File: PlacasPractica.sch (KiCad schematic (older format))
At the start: 66 parts, among them J1 USB_OTG, J2 Conn_01x10, J3 Conn_01x10, J4 CONN_02X05, SW1 SW_Push, U1 SAMD20J18A-AU, U2 XBEE, U3 MB85RC64VPNF-G-JNERE1, U4 XC6220B331MR-G, U5 XC6220B331MR-G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

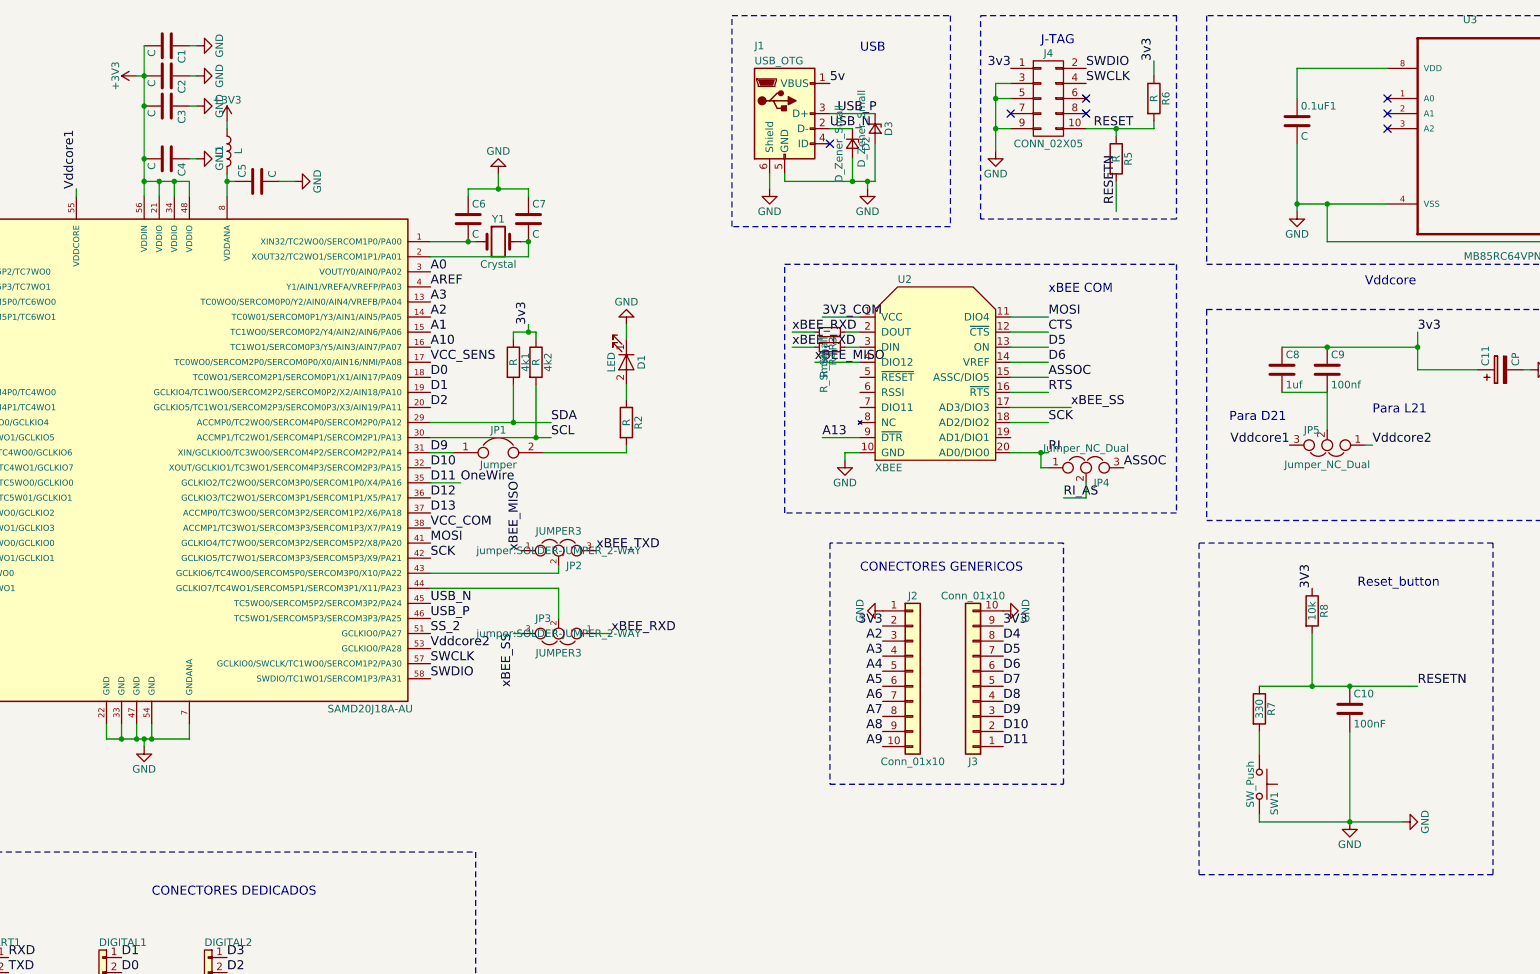
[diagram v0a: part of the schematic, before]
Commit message: Inicio diseño PCB
Se ha iniciado con el diseño de la PCB
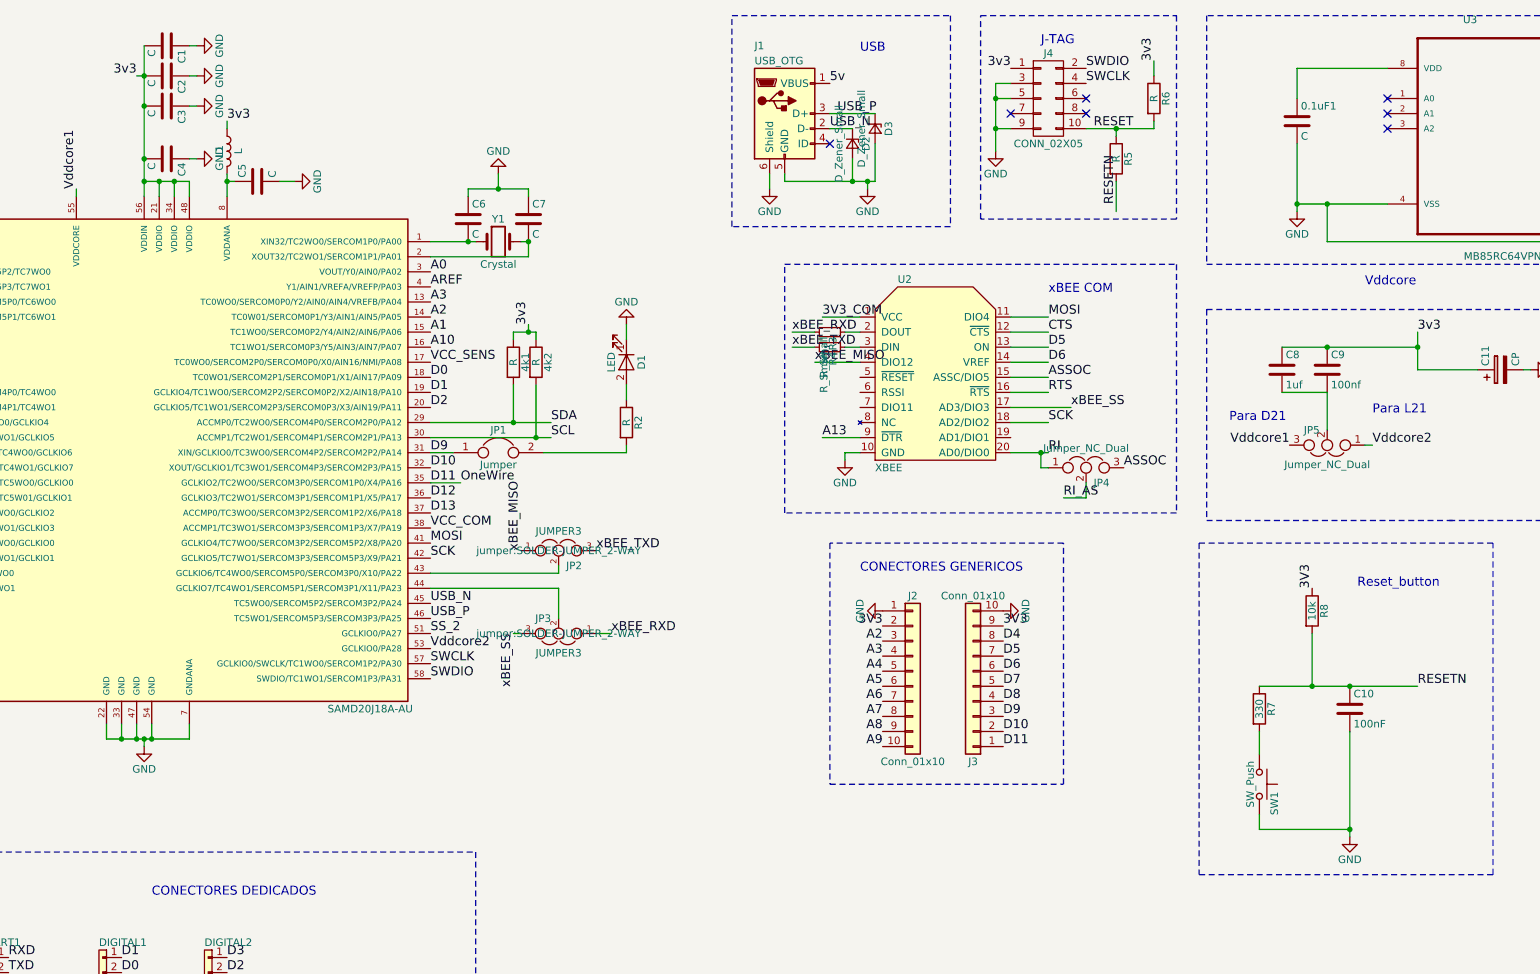
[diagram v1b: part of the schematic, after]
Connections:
- net +3V3 is gone; now on net 3v3: C1.2, C2.2, C3.2, C4.2, L1.1, U1.21 (VDDIO), U1.34 (VDDIO), U1.48 (VDDIO), U1.56 (VDDIN)
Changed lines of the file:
@@
 LIBS:valves
 LIBS:switches
-LIBS:ICs
 LIBS:PlacasPractica-cache
 EELAYER 25 0
@@
 	1    3500 1700
 	0    -1   -1   0
-$EndComp
-$Comp
-L +3V3 #PWR010
-U 1 1 59060D57
-P 2450 1000
-F 0 "#PWR010" H 2450 850 50  0001 C CNN
-F 1 "+3V3" H 2450 1140 50  0000 C CNN
-F 2 "" H 2450 1000 50  0001 C CNN
-F 3 "" H 2450 1000 50  0001 C CNN
-	1    2450 1000
-	0    -1   -1   0
-$EndComp
-$Comp
-L +3V3 #PWR011
-U 1 1 59060D58
-P 3050 1300
-F 0 "#PWR011" H 3050 1150 50  0001 C CNN
-F 1 "+3V3" H 3050 1440 50  0000 C CNN
-F 2 "" H 3050 1300 50  0001 C CNN
-F 3 "" H 3050 1300 50  0001 C CNN
-	1    3050 1300
-	1    0    0    -1
 $EndComp
 Text Label 4400 2300 0    60   ~ 0
@@
 J-TAG
 $Comp
-L GND #PWR012
+L GND #PWR011
 U 1 1 59060D6D
 P 7300 1750
-F 0 "#PWR012" H 7300 1500 50  0001 C CNN
+F 0 "#PWR011" H 7300 1500 50  0001 C CNN
 F 1 "GND" H 7300 1600 50  0000 C CNN
 F 2 "" H 7300 1750 50  0001 C CNN
@@
 USB
 $Comp
-L GND #PWR013
+L GND #PWR012
 U 1 1 59060D71
 P 6650 1750
-F 0 "#PWR013" H 6650 1500 50  0001 C CNN
+F 0 "#PWR012" H 6650 1500 50  0001 C CNN
 F 1 "GND" H 6650 1600 50  0000 C CNN
 F 2 "" H 6650 1750 50  0001 C CNN
@@
 xBEE_MISO
 $Comp
-L GND #PWR014
+L GND #PWR013
 U 1 1 59060D75
 P 7150 3550
-F 0 "#PWR014" H 7150 3300 50  0001 C CNN
+F 0 "#PWR013" H 7150 3300 50  0001 C CNN
 F 1 "GND" H 7150 3400 50  0000 C CNN
 F 2 "" H 7150 3550 50  0001 C CNN
@@
 3V3_SENS
 $Comp
-L GND #PWR015
+L GND #PWR014
 U 1 1 59060D81
 P 1600 7150
-F 0 "#PWR015" H 1600 6900 50  0001 C CNN
+F 0 "#PWR014" H 1600 6900 50  0001 C CNN
 F 1 "GND" H 1600 7000 50  0000 C CNN
 F 2 "" H 1600 7150 50  0001 C CNN
@@
 $EndComp
 $Comp
-L GND #PWR016
+L GND #PWR015
 U 1 1 59060D82
 P 1600 7950
-F 0 "#PWR016" H 1600 7700 50  0001 C CNN
+F 0 "#PWR015" H 1600 7700 50  0001 C CNN
 F 1 "GND" H 1600 7800 50  0000 C CNN
 F 2 "" H 1600 7950 50  0001 C CNN
@@
 	9200 1000 9200 900
 $Comp
-L GND #PWR017
+L GND #PWR016
 U 1 1 59094656
 P 8150 1500
-F 0 "#PWR017" H 8150 1250 50  0001 C CNN
+F 0 "#PWR016" H 8150 1250 50  0001 C CNN
 F 1 "GND" H 8150 1350 50  0000 C CNN
 F 2 "" H 8150 1500 50  0000 C CNN
@@
 $EndComp
 $Comp
-L GND #PWR018
+L GND #PWR017
 U 1 1 5AB3C19A
 P 10150 1900
-F 0 "#PWR018" H 10150 1650 50  0001 C CNN
+F 0 "#PWR017" H 10150 1650 50  0001 C CNN
 F 1 "GND" H 10150 1750 50  0000 C CNN
 F 2 "" H 10150 1900 50  0001 C CNN
@@
 $EndComp
 $Comp
-L GND #PWR019
+L GND #PWR018
 U 1 1 5AB3DAE7
 P 13650 3200
-F 0 "#PWR019" H 13650 2950 50  0001 C CNN
+F 0 "#PWR018" H 13650 2950 50  0001 C CNN
 F 1 "GND" H 13650 3050 50  0000 C CNN
 F 2 "" H 13650 3200 50  0001 C CNN
@@
 VCC_SENS
 $Comp
-L GND #PWR020
+L GND #PWR019
 U 1 1 5AB3DAEE
 P 14200 3200
-F 0 "#PWR020" H 14200 2950 50  0001 C CNN
+F 0 "#PWR019" H 14200 2950 50  0001 C CNN
 F 1 "GND" H 14200 3050 50  0000 C CNN
 F 2 "" H 14200 3200 50  0001 C CNN
@@
 $EndComp
 $Comp
-L GND #PWR021
+L GND #PWR020
 U 1 1 5AB3DAF4
 P 15800 3000
-F 0 "#PWR021" H 15800 2750 50  0001 C CNN
+F 0 "#PWR020" H 15800 2750 50  0001 C CNN
 F 1 "GND" H 15800 2850 50  0000 C CNN
 F 2 "" H 15800 3000 50  0001 C CNN
@@
 Connection ~ 15800 2600
 $Comp
-L +5V #PWR022
+L +5V #PWR021
 U 1 1 5AB3DADB
 P 12900 2500
-F 0 "#PWR022" H 12900 2350 50  0001 C CNN
+F 0 "#PWR021" H 12900 2350 50  0001 C CNN
 F 1 "+5V" H 12900 2640 50  0000 C CNN
 F 2 "" H 12900 2500 50  0001 C CNN
@@
 $EndComp
 $Comp
-L GND #PWR023
+L GND #PWR022
 U 1 1 5AB3F521
 P 14000 1700
-F 0 "#PWR023" H 14000 1450 50  0001 C CNN
+F 0 "#PWR022" H 14000 1450 50  0001 C CNN
 F 1 "GND" H 14000 1550 50  0000 C CNN
 F 2 "" H 14000 1700 50  0001 C CNN
@@
 $EndComp
 $Comp
-L GND #PWR024
+L GND #PWR023
 U 1 1 5AB3F527
 P 15800 1500
-F 0 "#PWR024" H 15800 1250 50  0001 C CNN
+F 0 "#PWR023" H 15800 1250 50  0001 C CNN
 F 1 "GND" H 15800 1350 50  0000 C CNN
 F 2 "" H 15800 1500 50  0001 C CNN
@@
 Connection ~ 15800 1100
 $Comp
-L +5V #PWR025
+L +5V #PWR024
 U 1 1 5AB3F545
 P 12950 850
-F 0 "#PWR025" H 12950 700 50  0001 C CNN
+F 0 "#PWR024" H 12950 700 50  0001 C CNN
 F 1 "+5V" H 12950 990 50  0000 C CNN
 F 2 "" H 12950 850 50  0001 C CNN
@@
 $EndComp
 $Comp
-L GND #PWR026
+L GND #PWR025
 U 1 1 5AB4419D
 P 13650 4700
-F 0 "#PWR026" H 13650 4450 50  0001 C CNN
+F 0 "#PWR025" H 13650 4450 50  0001 C CNN
 F 1 "GND" H 13650 4550 50  0000 C CNN
 F 2 "" H 13650 4700 50  0001 C CNN
@@
 VCC_COM
 $Comp
-L GND #PWR027
+L GND #PWR026
 U 1 1 5AB441A4
 P 14200 4700
-F 0 "#PWR027" H 14200 4450 50  0001 C CNN
+F 0 "#PWR026" H 14200 4450 50  0001 C CNN
 F 1 "GND" H 14200 4550 50  0000 C CNN
 F 2 "" H 14200 4700 50  0001 C CNN
@@
 $EndComp
 $Comp
-L GND #PWR028
+L GND #PWR027
 U 1 1 5AB441AA
 P 15800 4500
-F 0 "#PWR028" H 15800 4250 50  0001 C CNN
+F 0 "#PWR027" H 15800 4250 50  0001 C CNN
 F 1 "GND" H 15800 4350 50  0000 C CNN
 F 2 "" H 15800 4500 50  0001 C CNN
@@
 Connection ~ 15800 4100
 $Comp
-L +5V #PWR029
+L +5V #PWR028
 U 1 1 5AB441C8
 P 12900 4000
-F 0 "#PWR029" H 12900 3850 50  0001 C CNN
+F 0 "#PWR028" H 12900 3850 50  0001 C CNN
 F 1 "+5V" H 12900 4140 50  0000 C CNN
 F 2 "" H 12900 4000 50  0001 C CNN
@@
 $EndComp
 $Comp
-L GND #PWR030
+L GND #PWR029
 U 1 1 5AB48687
 P 3750 7950
-F 0 "#PWR030" H 3750 7700 50  0001 C CNN
+F 0 "#PWR029" H 3750 7700 50  0001 C CNN
 F 1 "GND" H 3750 7800 50  0000 C CNN
 F 2 "" H 3750 7950 50  0001 C CNN
@@
 $EndComp
 $Comp
-L GND #PWR031
+L GND #PWR030
 U 1 1 5AB4B4A0
 P 2350 7950
-F 0 "#PWR031" H 2350 7700 50  0001 C CNN
+F 0 "#PWR030" H 2350 7700 50  0001 C CNN
 F 1 "GND" H 2350 7800 50  0000 C CNN
 F 2 "" H 2350 7950 50  0001 C CNN
@@
 $EndComp
 $Comp
-L GND #PWR032
+L GND #PWR031
 U 1 1 5AB4BF34
 P 3050 7950
-F 0 "#PWR032" H 3050 7700 50  0001 C CNN
+F 0 "#PWR031" H 3050 7700 50  0001 C CNN
 F 1 "GND" H 3050 7800 50  0000 C CNN
 F 2 "" H 3050 7950 50  0001 C CNN
@@
 $EndComp
 $Comp
-L GND #PWR033
+L GND #PWR032
 U 1 1 5AB4C1E2
 P 2350 7150
-F 0 "#PWR033" H 2350 6900 50  0001 C CNN
+F 0 "#PWR032" H 2350 6900 50  0001 C CNN
 F 1 "GND" H 2350 7000 50  0000 C CNN
 F 2 "" H 2350 7150 50  0001 C CNN
@@
 $EndComp
 $Comp
-L GND #PWR034
+L GND #PWR033
 U 1 1 5AB4CC9B
 P 3050 7150
-F 0 "#PWR034" H 3050 6900 50  0001 C CNN
+F 0 "#PWR033" H 3050 6900 50  0001 C CNN
 F 1 "GND" H 3050 7000 50  0000 C CNN
 F 2 "" H 3050 7150 50  0001 C CNN
@@
 	1    0    0    -1
 $EndComp
-$Comp
-L GND #PWR035
-U 1 1 5AB40006
-P 10500 5950
-F 0 "#PWR035" H 10500 5700 50  0001 C CNN
-F 1 "GND" H 10500 5800 50  0000 C CNN
-F 2 "" H 10500 5950 50  0001 C CNN
-F 3 "" H 10500 5950 50  0001 C CNN
-	1    10500 5950
-	1    0    0    -1
-$EndComp
-$Comp
-L GND #PWR036
-U 1 1 5AB40094
-P 10850 5950
-F 0 "#PWR036" H 10850 5700 50  0001 C CNN
-F 1 "GND" H 10850 5800 50  0000 C CNN
-F 2 "" H 10850 5950 50  0001 C CNN
-F 3 "" H 10850 5950 50  0001 C CNN
-	1    10850 5950
-	0    -1   -1   0
-$EndComp
 Wire Wire Line
 	10250 4700 10250 5050
@@
 	9900 5350 9900 5500
 Wire Wire Line
-	9900 5900 9900 5950
-Wire Wire Line
-	9900 5950 10850 5950
-Connection ~ 10500 5950
-Wire Wire Line
-	10500 5350 10500 5950
+	9900 5900 9900 6000
+Wire Wire Line
+	10500 5350 10500 6050
 Text Label 10250 4400 1    60   ~ 0
 3V3
@@
 $EndComp
 $Comp
-L GND #PWR037
+L GND #PWR036
 U 1 1 5AB46D5A
 P 8200 4550
-F 0 "#PWR037" H 8200 4300 50  0001 C CNN
+F 0 "#PWR036" H 8200 4300 50  0001 C CNN
 F 1 "GND" H 8200 4400 50  0000 C CNN
 F 2 "" H 8200 4550 50  0001 C CNN
@@
 $EndComp
 $Comp
-L GND #PWR038
+L GND #PWR037
 U 1 1 5AB470E5
 P 7400 4550
-F 0 "#PWR038" H 7400 4300 50  0001 C CNN
+F 0 "#PWR037" H 7400 4300 50  0001 C CNN
 F 1 "GND" H 7400 4400 50  0000 C CNN
 F 2 "" H 7400 4550 50  0001 C CNN
@@
 Wire Notes Line
 	11900 3950 11150 3950
+Text Label 2450 1000 2    60   ~ 0
+3v3
+Text Label 3050 1300 0    60   ~ 0
+3v3
+$Comp
+L GND #PWR034
+U 1 1 5AB40006
+P 10500 6050
+F 0 "#PWR034" H 10500 5800 50  0001 C CNN
+F 1 "GND" H 10500 5900 50  0000 C CNN
+F 2 "" H 10500 6050 50  0001 C CNN
+F 3 "" H 10500 6050 50  0001 C CNN
+	1    10500 6050
+	1    0    0    -1
+$EndComp
+Wire Wire Line
+	10500 6000 9900 6000
+Connection ~ 10500 6000
 $EndSCHEMATC

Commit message: Diseño pcb, punto intermedio.
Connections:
- net 5v is gone; now on net +5V: J1.1 (VBUS)
- net 3V3: now also 0.1uF1.1, U3.8 (VDD)
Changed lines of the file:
@@
 LIBS:valves
 LIBS:switches
+LIBS:ICs
 LIBS:PlacasPractica-cache
 EELAYER 25 0
@@
 J-TAG
 $Comp
-L GND #PWR011
+L GND #PWR010
 U 1 1 59060D6D
 P 7300 1750
-F 0 "#PWR011" H 7300 1500 50  0001 C CNN
+F 0 "#PWR010" H 7300 1500 50  0001 C CNN
 F 1 "GND" H 7300 1600 50  0000 C CNN
 F 2 "" H 7300 1750 50  0001 C CNN
@@
 USB_N
 NoConn ~ 7050 1450
-Text Label 7050 1050 0    60   ~ 0
-5v
 Text Notes 7250 850  0    60   ~ 0
 USB
 $Comp
-L GND #PWR012
+L GND #PWR011
 U 1 1 59060D71
 P 6650 1750
-F 0 "#PWR012" H 6650 1500 50  0001 C CNN
+F 0 "#PWR011" H 6650 1500 50  0001 C CNN
 F 1 "GND" H 6650 1600 50  0000 C CNN
 F 2 "" H 6650 1750 50  0001 C CNN
@@
 xBEE_MISO
 $Comp
-L GND #PWR013
+L GND #PWR012
 U 1 1 59060D75
 P 7150 3550
-F 0 "#PWR013" H 7150 3300 50  0001 C CNN
+F 0 "#PWR012" H 7150 3300 50  0001 C CNN
 F 1 "GND" H 7150 3400 50  0000 C CNN
 F 2 "" H 7150 3550 50  0001 C CNN
@@
 3V3_SENS
 $Comp
-L GND #PWR014
+L GND #PWR013
 U 1 1 59060D81
 P 1600 7150
-F 0 "#PWR014" H 1600 6900 50  0001 C CNN
+F 0 "#PWR013" H 1600 6900 50  0001 C CNN
 F 1 "GND" H 1600 7000 50  0000 C CNN
 F 2 "" H 1600 7150 50  0001 C CNN
@@
 $EndComp
 $Comp
-L GND #PWR015
+L GND #PWR014
 U 1 1 59060D82
 P 1600 7950
-F 0 "#PWR015" H 1600 7700 50  0001 C CNN
+F 0 "#PWR014" H 1600 7700 50  0001 C CNN
 F 1 "GND" H 1600 7800 50  0000 C CNN
 F 2 "" H 1600 7950 50  0001 C CNN
@@
 	9200 1000 9200 900
 $Comp
-L GND #PWR016
+L GND #PWR015
 U 1 1 59094656
 P 8150 1500
-F 0 "#PWR016" H 8150 1250 50  0001 C CNN
+F 0 "#PWR015" H 8150 1250 50  0001 C CNN
 F 1 "GND" H 8150 1350 50  0000 C CNN
 F 2 "" H 8150 1500 50  0000 C CNN
@@
 $EndComp
 $Comp
-L GND #PWR017
+L GND #PWR016
 U 1 1 5AB3C19A
 P 10150 1900
-F 0 "#PWR017" H 10150 1650 50  0001 C CNN
+F 0 "#PWR016" H 10150 1650 50  0001 C CNN
 F 1 "GND" H 10150 1750 50  0000 C CNN
 F 2 "" H 10150 1900 50  0001 C CNN
@@
 $EndComp
 $Comp
-L GND #PWR018
+L GND #PWR017
 U 1 1 5AB3DAE7
 P 13650 3200
-F 0 "#PWR018" H 13650 2950 50  0001 C CNN
+F 0 "#PWR017" H 13650 2950 50  0001 C CNN
 F 1 "GND" H 13650 3050 50  0000 C CNN
 F 2 "" H 13650 3200 50  0001 C CNN
@@
 VCC_SENS
 $Comp
-L GND #PWR019
+L GND #PWR018
 U 1 1 5AB3DAEE
 P 14200 3200
-F 0 "#PWR019" H 14200 2950 50  0001 C CNN
+F 0 "#PWR018" H 14200 2950 50  0001 C CNN
 F 1 "GND" H 14200 3050 50  0000 C CNN
 F 2 "" H 14200 3200 50  0001 C CNN
@@
 $EndComp
 $Comp
-L GND #PWR020
+L GND #PWR019
 U 1 1 5AB3DAF4
 P 15800 3000
-F 0 "#PWR020" H 15800 2750 50  0001 C CNN
+F 0 "#PWR019" H 15800 2750 50  0001 C CNN
 F 1 "GND" H 15800 2850 50  0000 C CNN
 F 2 "" H 15800 3000 50  0001 C CNN
@@
 Connection ~ 15800 2600
 $Comp
-L +5V #PWR021
+L +5V #PWR020
 U 1 1 5AB3DADB
 P 12900 2500
-F 0 "#PWR021" H 12900 2350 50  0001 C CNN
+F 0 "#PWR020" H 12900 2350 50  0001 C CNN
 F 1 "+5V" H 12900 2640 50  0000 C CNN
 F 2 "" H 12900 2500 50  0001 C CNN
@@
 $EndComp
 $Comp
-L GND #PWR022
+L GND #PWR021
 U 1 1 5AB3F521
 P 14000 1700
-F 0 "#PWR022" H 14000 1450 50  0001 C CNN
+F 0 "#PWR021" H 14000 1450 50  0001 C CNN
 F 1 "GND" H 14000 1550 50  0000 C CNN
 F 2 "" H 14000 1700 50  0001 C CNN
@@
 $EndComp
 $Comp
-L GND #PWR023
+L GND #PWR022
 U 1 1 5AB3F527
 P 15800 1500
-F 0 "#PWR023" H 15800 1250 50  0001 C CNN
+F 0 "#PWR022" H 15800 1250 50  0001 C CNN
 F 1 "GND" H 15800 1350 50  0000 C CNN
 F 2 "" H 15800 1500 50  0001 C CNN
@@
 Connection ~ 15800 1100
 $Comp
-L +5V #PWR024
+L +5V #PWR023
 U 1 1 5AB3F545
 P 12950 850
-F 0 "#PWR024" H 12950 700 50  0001 C CNN
+F 0 "#PWR023" H 12950 700 50  0001 C CNN
 F 1 "+5V" H 12950 990 50  0000 C CNN
 F 2 "" H 12950 850 50  0001 C CNN
@@
 $EndComp
 $Comp
-L GND #PWR025
+L GND #PWR024
 U 1 1 5AB4419D
 P 13650 4700
-F 0 "#PWR025" H 13650 4450 50  0001 C CNN
+F 0 "#PWR024" H 13650 4450 50  0001 C CNN
 F 1 "GND" H 13650 4550 50  0000 C CNN
 F 2 "" H 13650 4700 50  0001 C CNN
@@
 VCC_COM
 $Comp
-L GND #PWR026
+L GND #PWR025
 U 1 1 5AB441A4
 P 14200 4700
-F 0 "#PWR026" H 14200 4450 50  0001 C CNN
+F 0 "#PWR025" H 14200 4450 50  0001 C CNN
 F 1 "GND" H 14200 4550 50  0000 C CNN
 F 2 "" H 14200 4700 50  0001 C CNN
@@
 $EndComp
 $Comp
-L GND #PWR027
+L GND #PWR026
 U 1 1 5AB441AA
 P 15800 4500
-F 0 "#PWR027" H 15800 4250 50  0001 C CNN
+F 0 "#PWR026" H 15800 4250 50  0001 C CNN
 F 1 "GND" H 15800 4350 50  0000 C CNN
 F 2 "" H 15800 4500 50  0001 C CNN
@@
 Connection ~ 15800 4100
 $Comp
-L +5V #PWR028
+L +5V #PWR027
 U 1 1 5AB441C8
 P 12900 4000
-F 0 "#PWR028" H 12900 3850 50  0001 C CNN
+F 0 "#PWR027" H 12900 3850 50  0001 C CNN
 F 1 "+5V" H 12900 4140 50  0000 C CNN
 F 2 "" H 12900 4000 50  0001 C CNN
@@
 $EndComp
 $Comp
-L GND #PWR029
+L GND #PWR028
 U 1 1 5AB48687
 P 3750 7950
-F 0 "#PWR029" H 3750 7700 50  0001 C CNN
+F 0 "#PWR028" H 3750 7700 50  0001 C CNN
 F 1 "GND" H 3750 7800 50  0000 C CNN
 F 2 "" H 3750 7950 50  0001 C CNN
@@
 $EndComp
 $Comp
-L GND #PWR030
+L GND #PWR029
 U 1 1 5AB4B4A0
 P 2350 7950
-F 0 "#PWR030" H 2350 7700 50  0001 C CNN
+F 0 "#PWR029" H 2350 7700 50  0001 C CNN
 F 1 "GND" H 2350 7800 50  0000 C CNN
 F 2 "" H 2350 7950 50  0001 C CNN
@@
 $EndComp
 $Comp
-L GND #PWR031
+L GND #PWR030
 U 1 1 5AB4BF34
 P 3050 7950
-F 0 "#PWR031" H 3050 7700 50  0001 C CNN
+F 0 "#PWR030" H 3050 7700 50  0001 C CNN
 F 1 "GND" H 3050 7800 50  0000 C CNN
 F 2 "" H 3050 7950 50  0001 C CNN
@@
 $EndComp
 $Comp
-L GND #PWR032
+L GND #PWR031
 U 1 1 5AB4C1E2
 P 2350 7150
-F 0 "#PWR032" H 2350 6900 50  0001 C CNN
+F 0 "#PWR031" H 2350 6900 50  0001 C CNN
 F 1 "GND" H 2350 7000 50  0000 C CNN
 F 2 "" H 2350 7150 50  0001 C CNN
@@
 $EndComp
 $Comp
-L GND #PWR033
+L GND #PWR032
 U 1 1 5AB4CC9B
 P 3050 7150
-F 0 "#PWR033" H 3050 6900 50  0001 C CNN
+F 0 "#PWR032" H 3050 6900 50  0001 C CNN
 F 1 "GND" H 3050 7000 50  0000 C CNN
 F 2 "" H 3050 7150 50  0001 C CNN
@@
 $EndComp
 $Comp
-L GND #PWR036
+L GND #PWR033
 U 1 1 5AB46D5A
 P 8200 4550
-F 0 "#PWR036" H 8200 4300 50  0001 C CNN
+F 0 "#PWR033" H 8200 4300 50  0001 C CNN
 F 1 "GND" H 8200 4400 50  0000 C CNN
 F 2 "" H 8200 4550 50  0001 C CNN
@@
 $EndComp
 $Comp
-L GND #PWR037
+L GND #PWR034
 U 1 1 5AB470E5
 P 7400 4550
-F 0 "#PWR037" H 7400 4300 50  0001 C CNN
+F 0 "#PWR034" H 7400 4300 50  0001 C CNN
 F 1 "GND" H 7400 4400 50  0000 C CNN
 F 2 "" H 7400 4550 50  0001 C CNN
@@
 3v3
 $Comp
-L GND #PWR034
+L GND #PWR035
 U 1 1 5AB40006
 P 10500 6050
-F 0 "#PWR034" H 10500 5800 50  0001 C CNN
+F 0 "#PWR035" H 10500 5800 50  0001 C CNN
 F 1 "GND" H 10500 5900 50  0000 C CNN
 F 2 "" H 10500 6050 50  0001 C CNN
@@
 $EndComp
 Wire Wire Line
-	10500 6000 9900 6000
+	9900 6000 10500 6000
 Connection ~ 10500 6000
+$Comp
+L +5V #PWR036
+U 1 1 5AB8F080
+P 7050 1050
+F 0 "#PWR036" H 7050 900 50  0001 C CNN
+F 1 "+5V" H 7050 1190 50  0000 C CNN
+F 2 "" H 7050 1050 50  0001 C CNN
+F 3 "" H 7050 1050 50  0001 C CNN
+	1    7050 1050
+	0    1    1    0
+$EndComp
+Text Label 10150 950  1    60   ~ 0
+3V3
 $EndSCHEMATC
